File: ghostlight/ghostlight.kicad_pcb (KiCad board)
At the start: 2 copper layers, 11 parts, among them IC1 STM32C011J4M6, IC2 MCP1700T-3302E_TT, IC3 LP5817DRLR

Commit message: added first board draft
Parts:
- BT1: moved to B.Cu
- moved BT1 30.9 mm to (155.0, 104.5), turned to 180 degrees
- moved C4 29.1 mm to (149.0, 95.5)
- moved C3 29.0 mm to (156.5, 96.0), turned to 180 degrees
- moved IC1 23.0 mm to (159.9, 100.3), turned to -90 degrees
- moved C1 22.0 mm to (150.7, 105.5)
- moved LED1 16.0 mm to (155.0, 100.0), turned to 90 degrees
- moved IC2 15.0 mm to (150.9, 101.0), turned to -90 degrees
- moved IC3 12.5 mm to (153.5, 94.8), turned to -90 degrees
- moved C2 10.0 mm to (149.3, 97.5), turned to 180 degrees
- moved R1 7.81 mm to (157.8, 94.5)
- moved R2 4.62 mm to (157.8, 93.0)
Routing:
- net 3.3V: track 0.00 -> 33.8 mm, vias 0 -> 3
- net V_BAT: track 0.00 -> 31.0 mm, vias 0 -> 4
- net SCK: track 0.00 -> 28.6 mm
- net ST_LINK_RST/RST: track 0.00 -> 14.1 mm
- net SDA: track 0.00 -> 13.4 mm
- net Net-(IC3-OUT2): track 0.00 -> 10.1 mm
- net GND: track 0.00 -> 9.72 mm, vias 0 -> 8
- net ST_LINK_SWDIO: track 0.00 -> 7.08 mm
- net Net-(IC3-OUT1): track 0.00 -> 6.66 mm
- net Net-(IC3-OUT0): track 0.00 -> 3.89 mm
- added copper zone on B.Cu, net GND
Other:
- board outline added: 25 x 25 mm

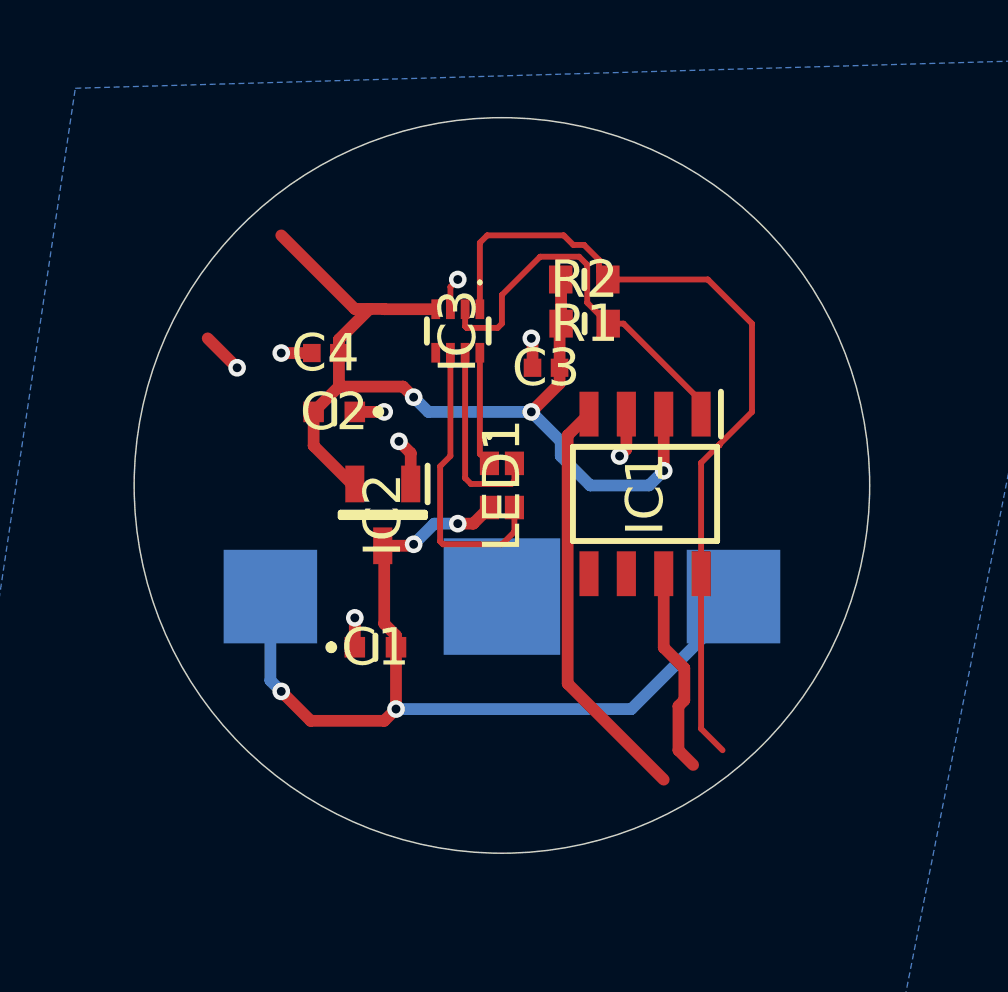
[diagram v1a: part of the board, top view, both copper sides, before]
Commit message: added custom ring for programming
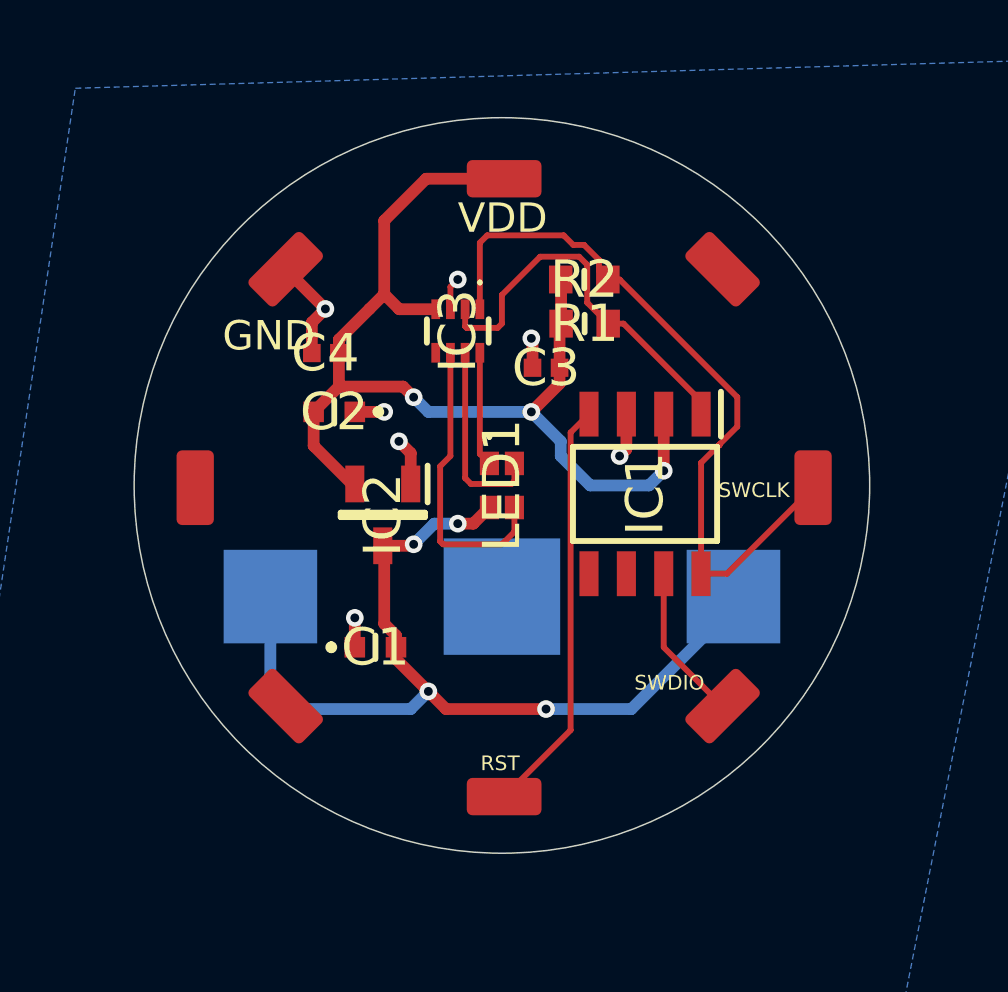
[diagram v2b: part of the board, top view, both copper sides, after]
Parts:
- added J1: Conn_01x08, custom_ring:Ring_connector_22mm, F.Cu at (155.1, 89.6)
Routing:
- net 3.3V: track 33.8 -> 37.4 mm
- net SCK: track 28.6 -> 25.2 mm
- net ST_LINK_SWDIO: track 7.08 -> 5.33 mm
- net GND: track 9.72 -> 10.9 mm, vias 8 -> 7
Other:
- board text added: "GND"
- board text added: "RST"
- board text added: "SWCLK"
- board text added: "SWDIO"
- board text added: "VDD"

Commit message: optimalized the PCB
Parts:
- moved C3 4.04 mm to (160.5, 96.0), turned to 0 degrees
- moved C4 1.80 mm to (150.5, 94.5)
- moved C1 1.04 mm to (151.0, 104.5)
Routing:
- net SDA: track 13.4 -> 16.2 mm
- net V_BAT: track 31.0 -> 28.7 mm
- net 3.3V: track 37.4 -> 36.1 mm, vias 3 -> 4
- net SCK: track 25.2 -> 26.3 mm
